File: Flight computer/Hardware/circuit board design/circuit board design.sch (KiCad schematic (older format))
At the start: 0 parts

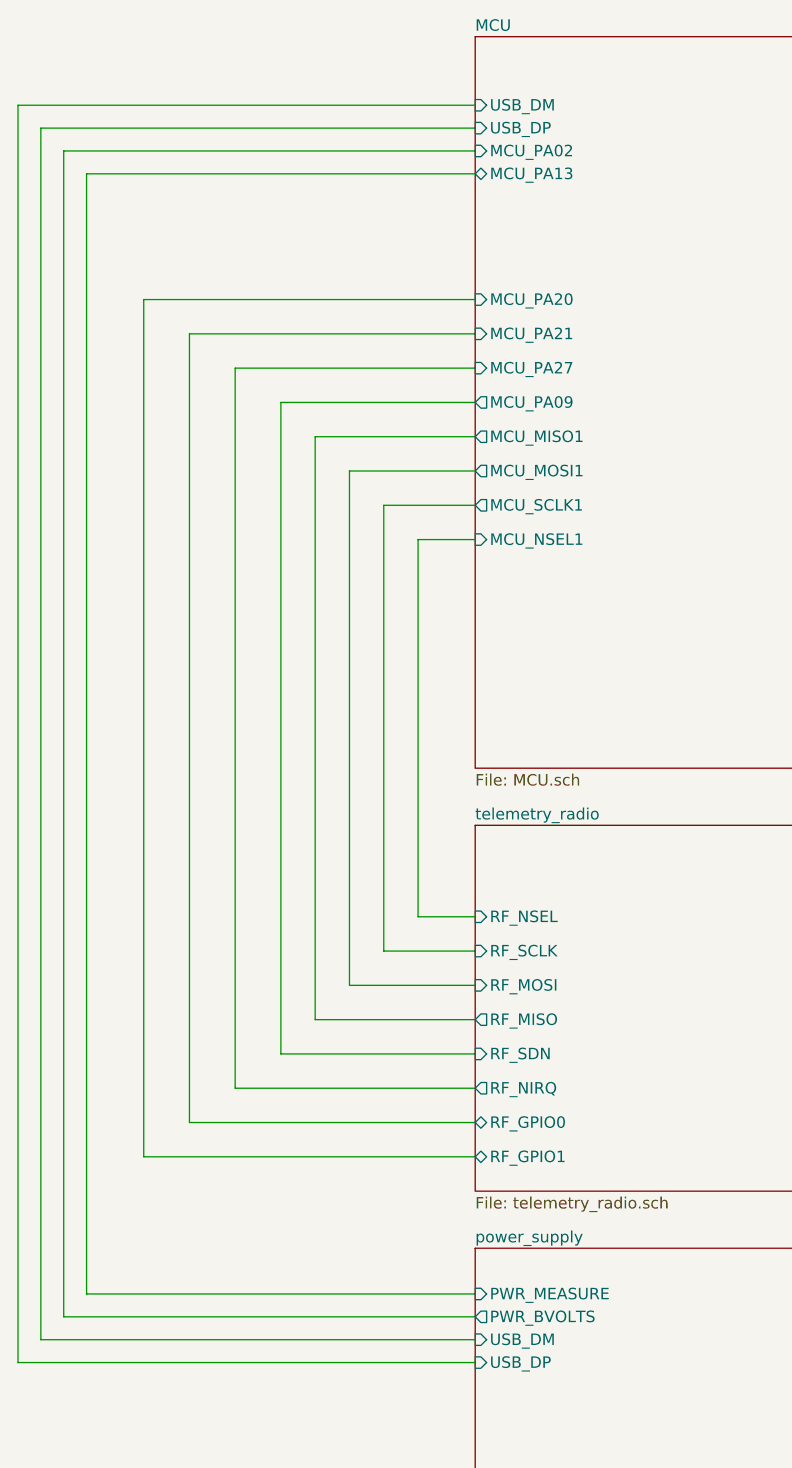
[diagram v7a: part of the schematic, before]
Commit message: fixed erc problems with Johanson integrated Frontend.
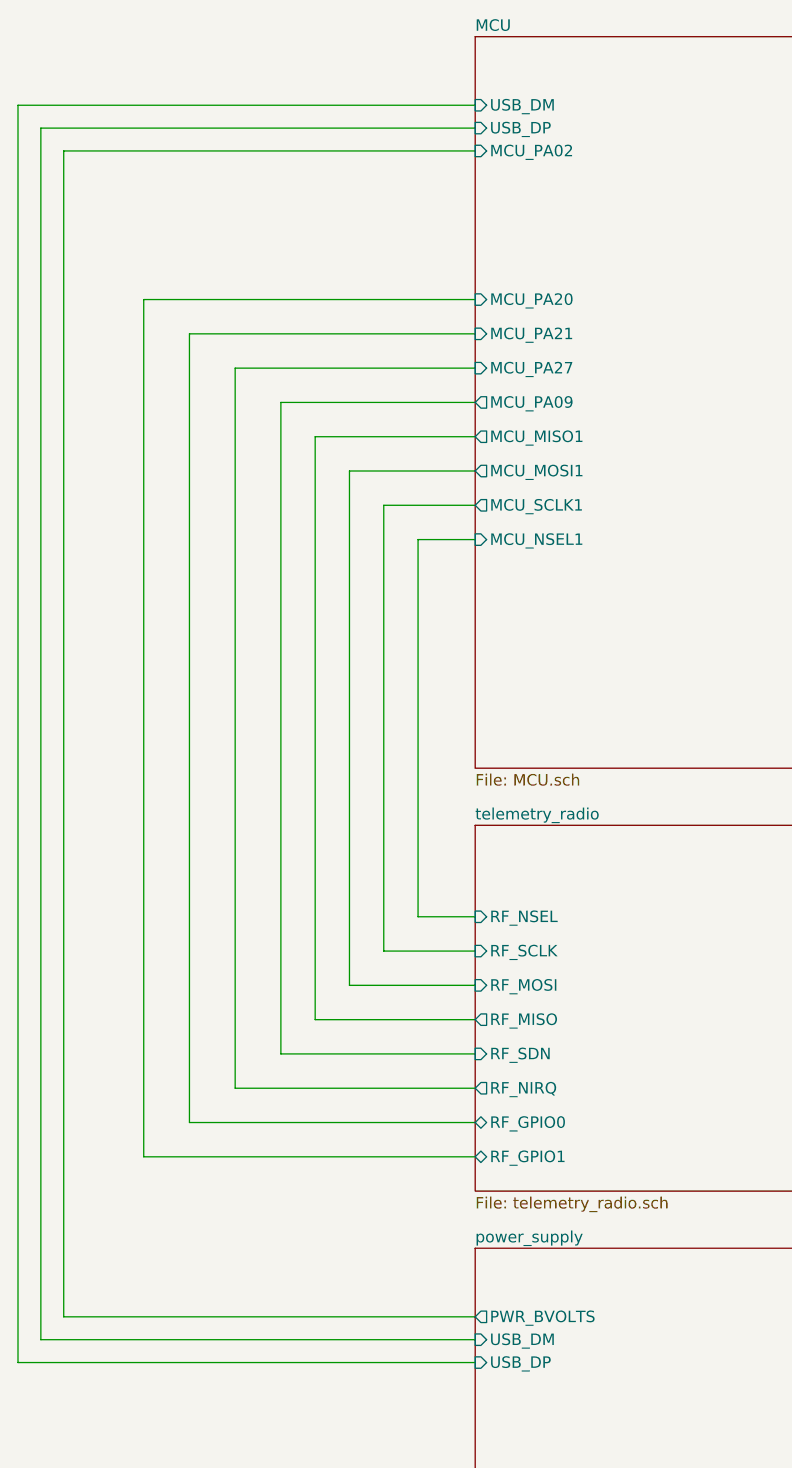
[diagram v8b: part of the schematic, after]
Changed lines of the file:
@@
 	7900 3900 6950 3900
-Wire Wire Line
-	1000 6600 2700 6600
-Wire Wire Line
-	1000 1700 1000 6600
 Wire Wire Line
 	2700 5700 1650 5700
@@
 	5050 2050 7900 2050
 Wire Wire Line
-	2700 1700 1000 1700
-Wire Wire Line
 	5050 3000 6550 3000
 Wire Wire Line
@@
 F13 "MCU_PA07" B R 5050 3000 50
 F14 "MCU_PA09" O L 2700 2700 50
-F15 "MCU_PA13" B L 2700 1700 50
-F16 "MCU_PB03" O R 5050 2050 50
-F17 "MCU_PB02" O R 5050 1600 50
-F18 "MCU_PB08" I R 5050 2200 50
-F19 "MCU_PA20" I L 2700 2250 50
-F20 "MCU_PA21" I L 2700 2400 50
-F21 "MCU_PA27" I L 2700 2550 50
-F22 "MCU_PB04" I R 5050 3250 50
-F23 "MCU_PB05" I R 5050 3350 50
-F24 "MCU_PB13" O R 5050 3700 50
-F25 "MCU_PB14" O R 5050 3800 50
-F26 "MCU_PB06" I R 5050 3450 50
-F27 "MCU_PB07" I R 5050 3550 50
-F28 "MCU_PB15" O R 5050 3900 50
-F29 "MCU_PB16" O R 5050 4000 50
-F30 "USB_DP" I L 2700 1500 50
-F31 "USB_DM" I L 2700 1400 50
+F15 "MCU_PB03" O R 5050 2050 50
+F16 "MCU_PB02" O R 5050 1600 50
+F17 "MCU_PB08" I R 5050 2200 50
+F18 "MCU_PA20" I L 2700 2250 50
+F19 "MCU_PA21" I L 2700 2400 50
+F20 "MCU_PA27" I L 2700 2550 50
+F21 "MCU_PB04" I R 5050 3250 50
+F22 "MCU_PB05" I R 5050 3350 50
+F23 "MCU_PB13" O R 5050 3700 50
+F24 "MCU_PB14" O R 5050 3800 50
+F25 "MCU_PB06" I R 5050 3450 50
+F26 "MCU_PB07" I R 5050 3550 50
+F27 "MCU_PB15" O R 5050 3900 50
+F28 "MCU_PB16" O R 5050 4000 50
+F29 "USB_DP" I L 2700 1500 50
+F30 "USB_DM" I L 2700 1400 50
 $EndSheet
 Wire Wire Line
@@
 F1 "power_supply.sch" 50
 F2 "PWR_BVOLTS" O L 2700 6700 50
-F3 "PWR_MEASURE" I L 2700 6600 50
-F4 "USB_DM" I L 2700 6800 50
-F5 "USB_DP" I L 2700 6900 50
+F3 "USB_DM" I L 2700 6800 50
+F4 "USB_DP" I L 2700 6900 50
 $EndSheet
 Wire Wire Line
